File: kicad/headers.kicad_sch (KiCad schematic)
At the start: 5 parts, among them J1 EX_IO1 (AXU3EGB J15), J2 EX_IO2 (AXU3EGB J16)

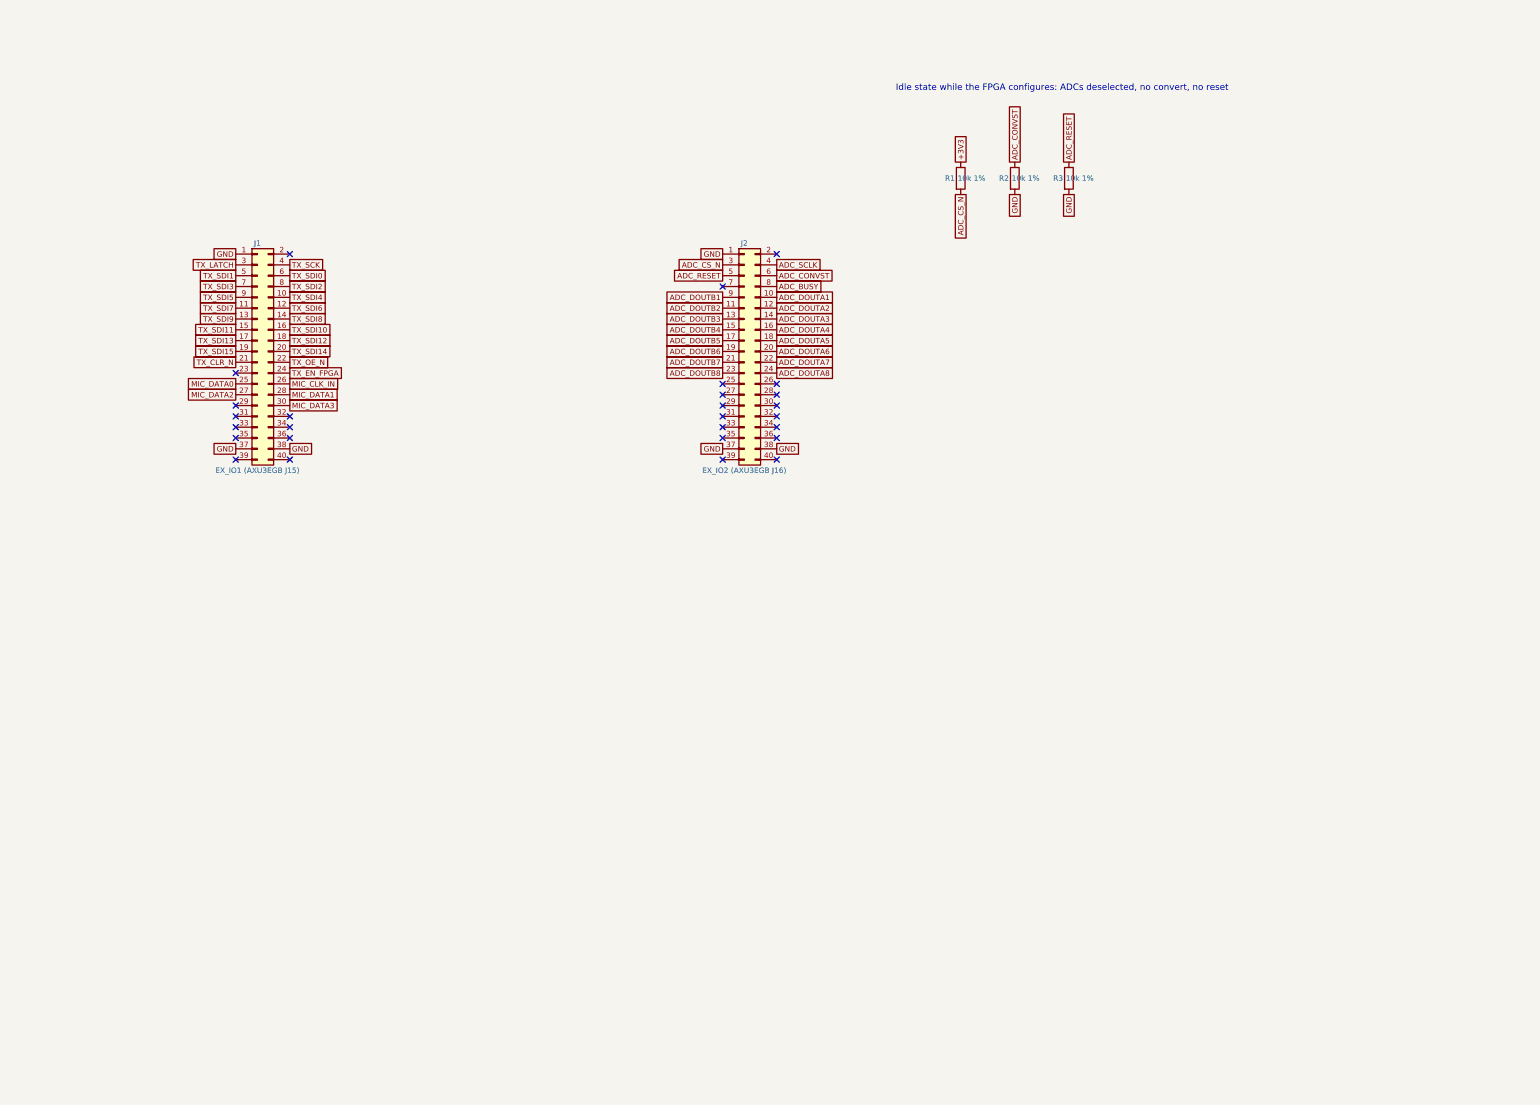
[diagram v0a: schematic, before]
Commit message: AD7606C-16, one sheet per repeated block, clock buffering, first simulations
- ADC: AD7606C-16 in software mode (OS pins high, WR held high, DB11/SDI on
  shared ADC_SDI), 33 R source resistors on DOUTA/DOUTB/BUSY.
- Every repeated block is its own reused sheet: tx_group x16, en_buf x4,
  clk_buf x7, mic x8 (replaces tx_shift, tx_drivers, mems). Sheets other than
  channel are generated by scripts/build_cells.py and scripts/build_power.py.
- Headers: GND conductors either side of every clock, ADC_SDI, idle pulls,
  DNP RC terminations as fallback.
- Power: 3V3_MIC ferrite filter moved to the power sheet with LED, test point
  and flag.
- Simulations (LTspice, sim/): RX chain gain/noise, TX burst and recovery,
  clock signal integrity; results in docs/simulation-1.md. FPGA ribbon outputs
  changed to DRIVE 4 after simulation.
- Brief, CLAUDE.md, review status and SKiDL reference spec updated.
  ERC: 0 violations, 1,701 parts.
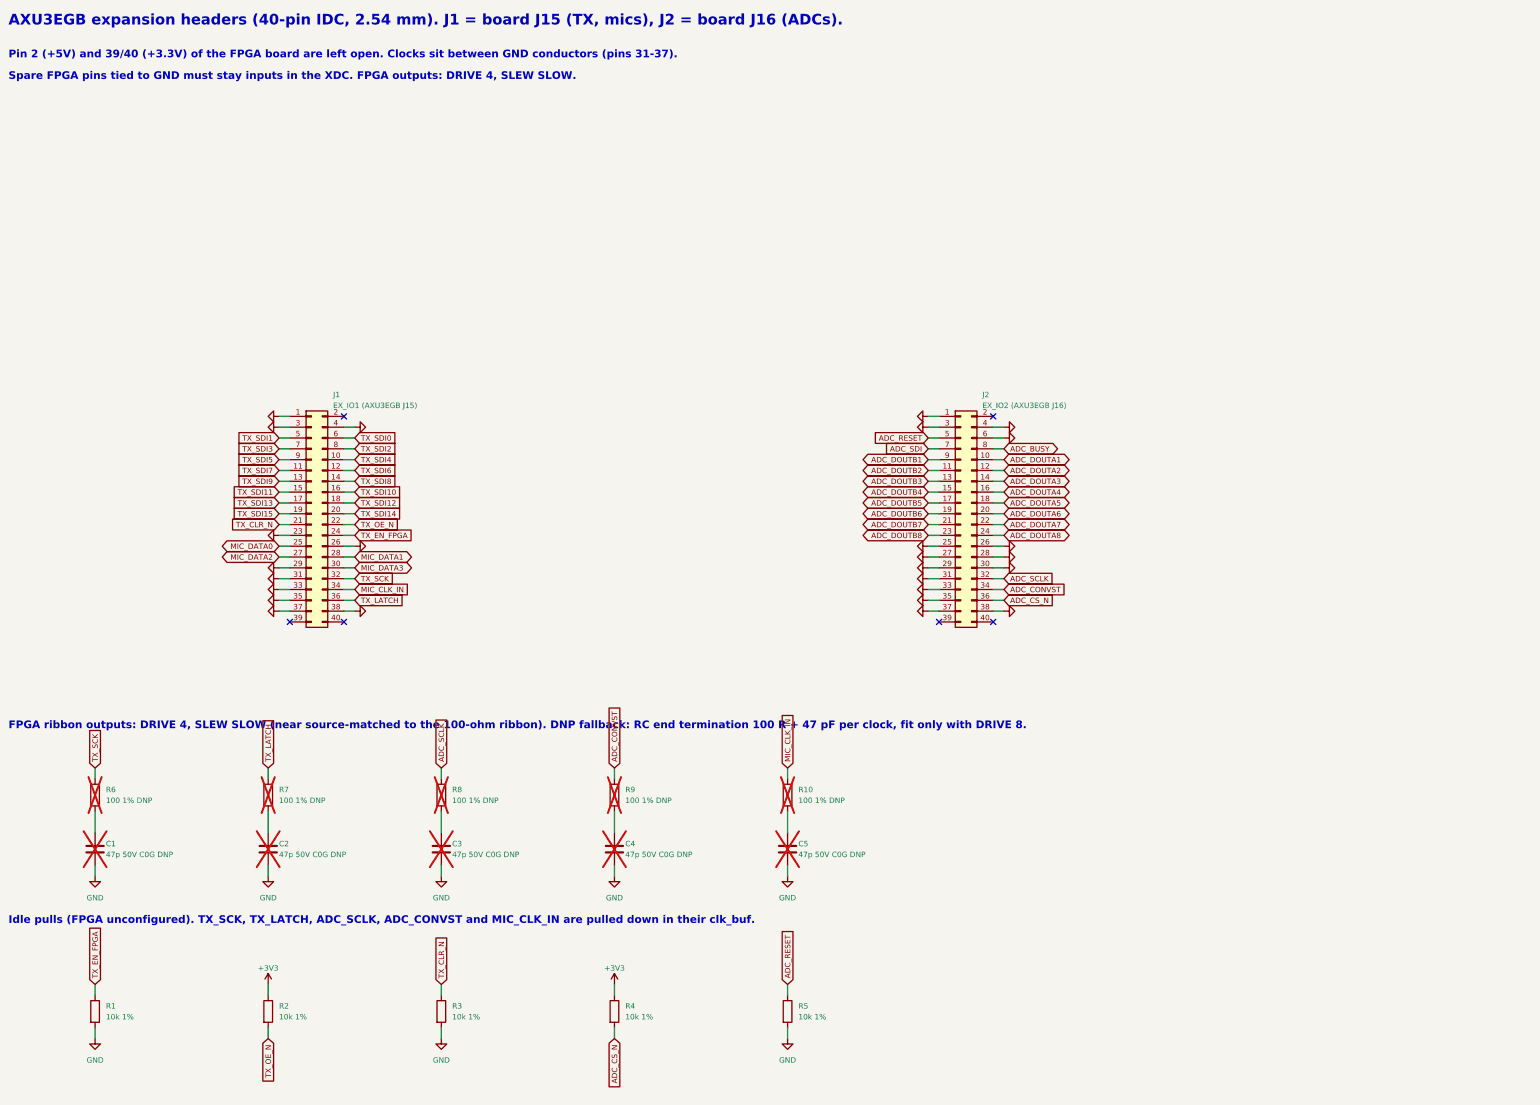
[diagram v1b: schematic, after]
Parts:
- added C1, C2, C3, C4, C5: 47p 50V C0G DNP, Capacitor_SMD:C_0603_1608Metric, symbol Device:C
- added R10, R6, R7, R8, R9: 100 1% DNP, Resistor_SMD:R_0603_1608Metric, symbol Device:R
- added R4, R5: 10k 1%, Resistor_SMD:R_0603_1608Metric, symbol Device:R
- R1, R2, R3: LCSC (none) -> TBD
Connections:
- net +3V3: now also R2.1, R4.1; no longer R1.1
- net ADC_CONVST: now also J2.34 (Pin_34), R9.1; no longer J2.6 (Pin_6), R2.1
- net ADC_CS_N: now also J2.36 (Pin_36), R4.2; no longer J2.3 (Pin_3), R1.2
- net ADC_RESET: now also R5.1; no longer R3.1
- net ADC_SCLK: now also J2.32 (Pin_32), R8.1; no longer J2.4 (Pin_4)
- net GND: now also J1.23 (Pin_23), J1.26 (Pin_26), J1.29 (Pin_29), J1.3 (Pin_3), J1.31 (Pin_31), J1.33 (Pin_33), J1.35 (Pin_35), J1.4 (Pin_4), J2.25 (Pin_25), J2.26 (Pin_26), J2.27 (Pin_27), J2.28 (Pin_28), J2.29 (Pin_29), J2.3 (Pin_3), J2.30 (Pin_30), J2.31 (Pin_31), J2.33 (Pin_33), J2.35 (Pin_35), J2.4 (Pin_4), J2.6 (Pin_6), R1.2, C1.2, C2.2, C3.2, C4.2, C5.2, R5.2; no longer R2.2
- net MIC_CLK_IN: now also J1.34 (Pin_34), R10.1; no longer J1.26 (Pin_26)
- net TX_CLR_N: now also R3.1
- net TX_EN_FPGA: now also R1.1
- net TX_LATCH: now also J1.36 (Pin_36), R7.1; no longer J1.3 (Pin_3)
- net TX_OE_N: now also R2.2
- net TX_SCK: now also J1.32 (Pin_32), R6.1; no longer J1.4 (Pin_4)
- net ADC_SDI: now reaches J2.7 (Pin_7)
- new net: C5.1, R10.2
- new net: C3.1, R8.2
- new net: C4.1, R9.2
- new net: C2.1, R7.2
- new net: C1.1, R6.2
- no-connect marks 27 -> 6
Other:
- note added: "AXU3EGB expansion headers (40-pin IDC, 2.54 mm). J1 = board J15 (TX, mics), J2 = board J16 (ADCs)."
- note added: "FPGA ribbon outputs: DRIVE 4, SLEW SLOW (near source-matched to the 100-ohm ribbon). DNP fallback: RC end termination 100 R + 47 pF per clock, fit only with DRIVE 8."
- note added: "Idle pulls (FPGA unconfigured). TX_SCK, TX_LATCH, ADC_SCLK, ADC_CONVST and MIC_CLK_IN are pulled down in their clk_buf."
- note added: "Pin 2 (+5V) and 39/40 (+3.3V) of the FPGA board are left open. Clocks sit between GND conductors (pins 31-37)."
- note added: "Spare FPGA pins tied to GND must stay inputs in the XDC. FPGA outputs: DRIVE 4, SLEW SLOW."
- note removed: "Idle state while the FPGA configures: ADCs deselected, no convert, no reset"

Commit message: Block-diagram top page, power review fixes, readable sheets
Top level
- Page 1 is now a block diagram of the signal flow (FPGA -> headers ->
  clock buffers / TX drive -> transceivers -> ADCs -> FPGA, mics, power).
- New group sheets hold the reused cells: tx (16 tx_group + 4 en_buf),
  array (64 channel), adcs (8 adc), mics (8 mic), clocks (7 clk_buf).
  Power and headers stay directly under the top. All written by gen_top.py,
  which now also survives a kicad-cli re-save of a cell sheet.

Power (review findings)
- Polyfuse 1812L200/16DR (16 V), TPS65131RGER stated explicitly, input caps
  2 x 10u 1206, 50 V caps on 12 V, inductor values carry minimum Isat.
- +3V3: TLV75733P (ceramic-stable) replaces TLV1117-33.
- New JP5/JP6 isolate +-6V5; every rail: REG node -> jumper -> rail with TP,
  LED (not on analog LDOs) and PWR_FLAG.
- Power sheet is now generated by build_cells.py in a 2x3 block layout
  (build_power.py removed).

Readability and small fixes
- Rails on sideways pins use labelled flags; sideways GND symbols hide text.
- tx_group: 595 outputs wired straight to the drivers.
- Title blocks on every sheet; channel sheet notes and field placement fixed
  (sch_fields.py --only, sch_annotate.py).
- ADC_SDI 10k pull-down, ADC reset/DOUT notes, mic cap 50 V.
- ERC 0 violations, 1,704 parts. PDFs: docs/schematics/00..13.
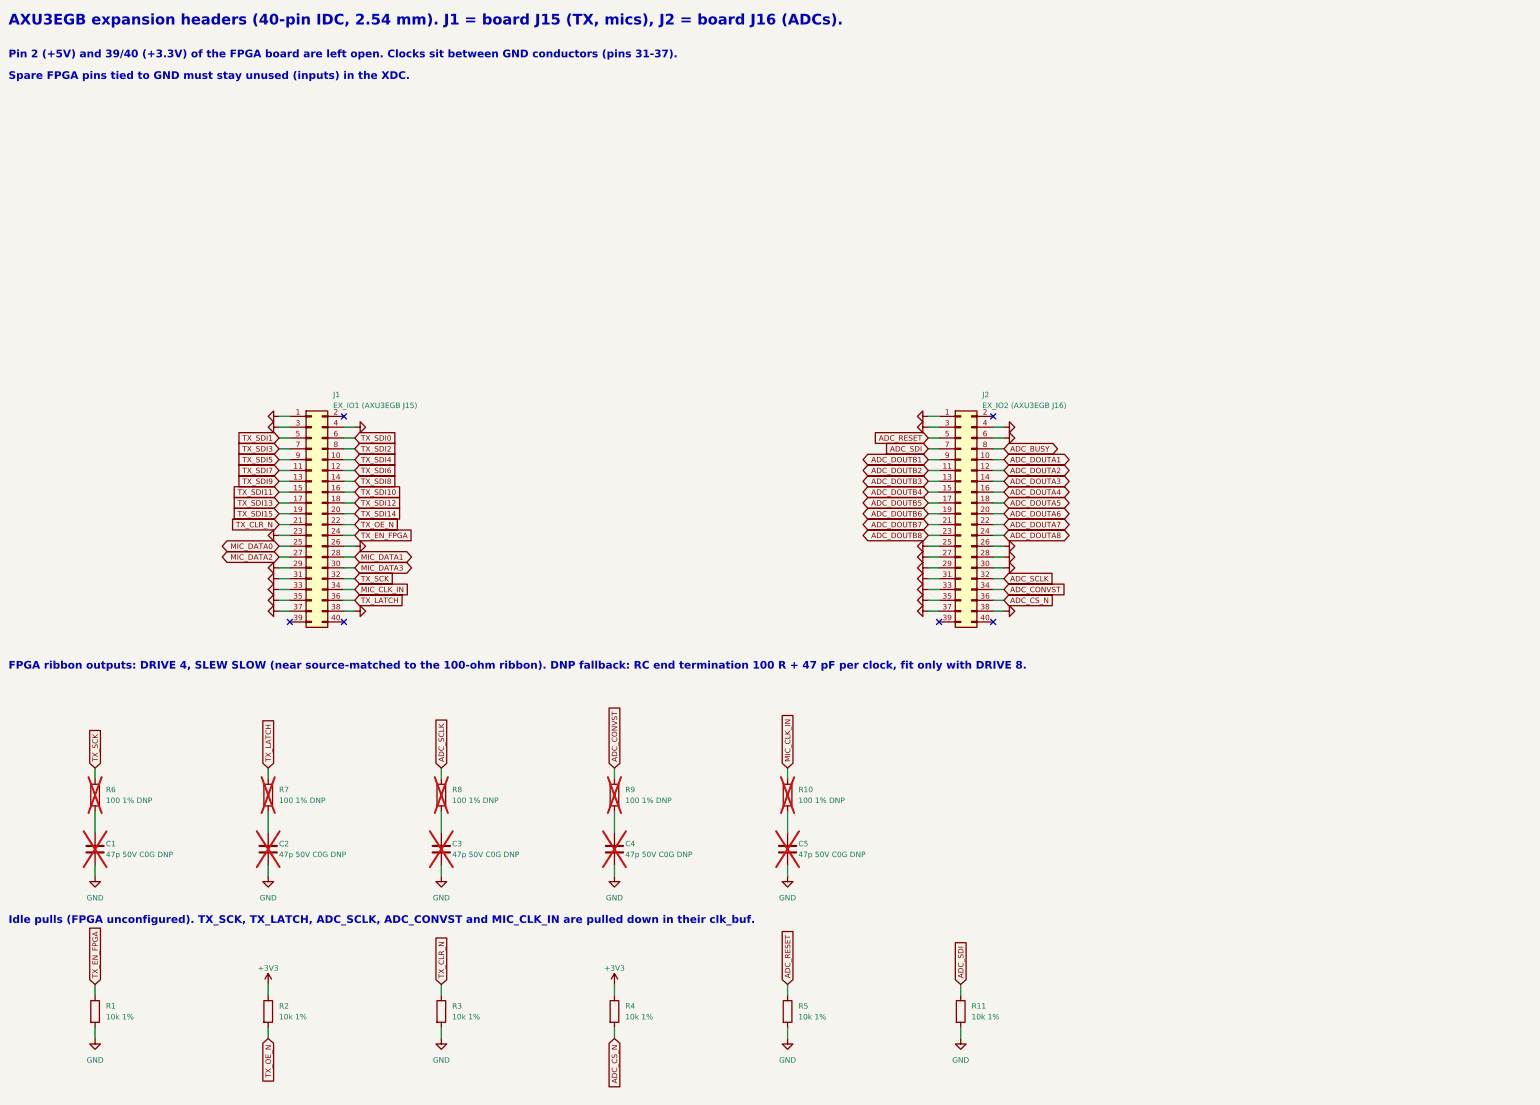
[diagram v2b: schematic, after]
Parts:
- added R11: 10k 1%, Resistor_SMD:R_0603_1608Metric, symbol Device:R
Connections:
- net ADC_SDI: now also R11.1
- net GND: now also R11.2
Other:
- note added: "Spare FPGA pins tied to GND must stay unused (inputs) in the XDC."
- note removed: "Spare FPGA pins tied to GND must stay inputs in the XDC. FPGA outputs: DRIVE 4, SLEW SLOW."
- company: (none) -> Hybrid 8x8 ultrasonic AESA
- title: (none) -> AXU3EGB headers J15/J16, idle pulls

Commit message: Optimized, costed BOM with LCSC numbers for every part
scripts/bom.py picks parts (Basic first, stock margin) and writes docs/bom.md,
fab/bom_jlcpcb.csv and scripts/parts.json; sch_lcsc.py fills LCSC fields from it.
Part changes: TPS7A4700RGWT for the out-of-stock TPS7A4701, BAV99 C2500, SS54 in SMA,
SMD1812P200TF16 polyfuse, 600R ferrite, Basic-value +5V/VDRV dividers (VDRV 15.4 V),
Sunlord SWPA6045 footprints, mic 100 nF C0G in 1206. AD7606C-16 and SPH0641 now
assembled by JLCPCB.
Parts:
- C1, C2, C3, C4, C5: LCSC TBD -> C1671 (DNP)
- J1, J2: LCSC TBD -> C19193815
- R1, R11, R2, R3, R4, R5: LCSC TBD -> C25804
- R10, R6, R7, R8, R9: LCSC TBD -> C22775 (DNP)
